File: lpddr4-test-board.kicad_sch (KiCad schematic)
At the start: 2 parts

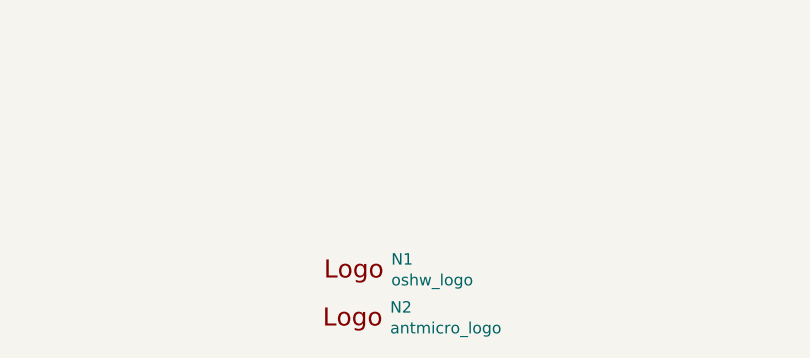
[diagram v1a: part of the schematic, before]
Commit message: Placement and routing of FT4232H. Re annotation of the schematics
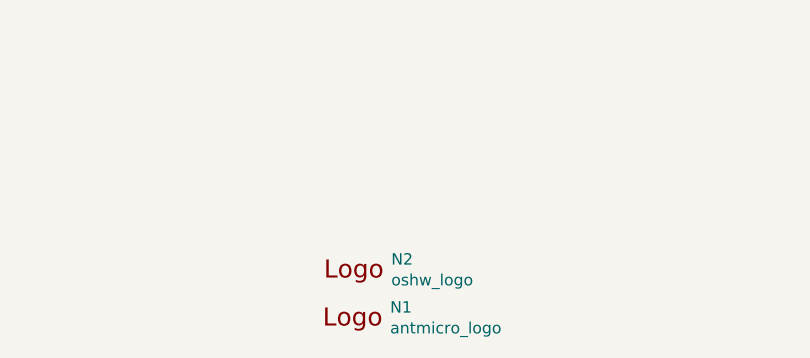
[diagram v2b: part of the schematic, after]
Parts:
- renumbered N2 to N1, N1 to N2
